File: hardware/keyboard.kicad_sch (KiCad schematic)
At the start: 65 parts, among them SW1 SW_Push, SW10 SW_Push, SW11 SW_Push, SW12 SW_Push, SW13 SW_Push, SW14 SW_Push, SW15 SW_Push, SW16 SW_Push, SW17 SW_Push, SW18 SW_Push, SW19 SW_Push, SW2 SW_Push, SW20 SW_Push, SW21 SW_Push, SW22 SW_Push, SW23 SW_Push, SW24 SW_Push, SW25 SW_Push, SW26 SW_Push, SW27 SW_Push, SW28 SW_Push, SW29 SW_Push, SW3 SW_Push, SW30 SW_Push, SW31 SW_Push, SW32 SW_Push, SW33 SW_Push, SW34 SW_Push, SW35 SW_Push, SW36 SW_Push, SW37 SW_Push, SW38 SW_Push, SW39 SW_Push, SW4 SW_Push, SW40 SW_Push, SW41 SW_Push, SW42 SW_Push, SW43 SW_Push, SW44 SW_Push, SW45 SW_Push, SW46 SW_Push, SW47 SW_Push, SW48 SW_Push, SW49 SW_Push, SW5 SW_Push, SW50 SW_Push, SW51 SW_Push, SW52 SW_Push, SW53 SW_Push, SW54 SW_Push, SW55 SW_Push, SW56 SW_Push, SW6 SW_Push, SW7 SW_Push, SW8 SW_Push, SW9 SW_Push, U2 74HC138

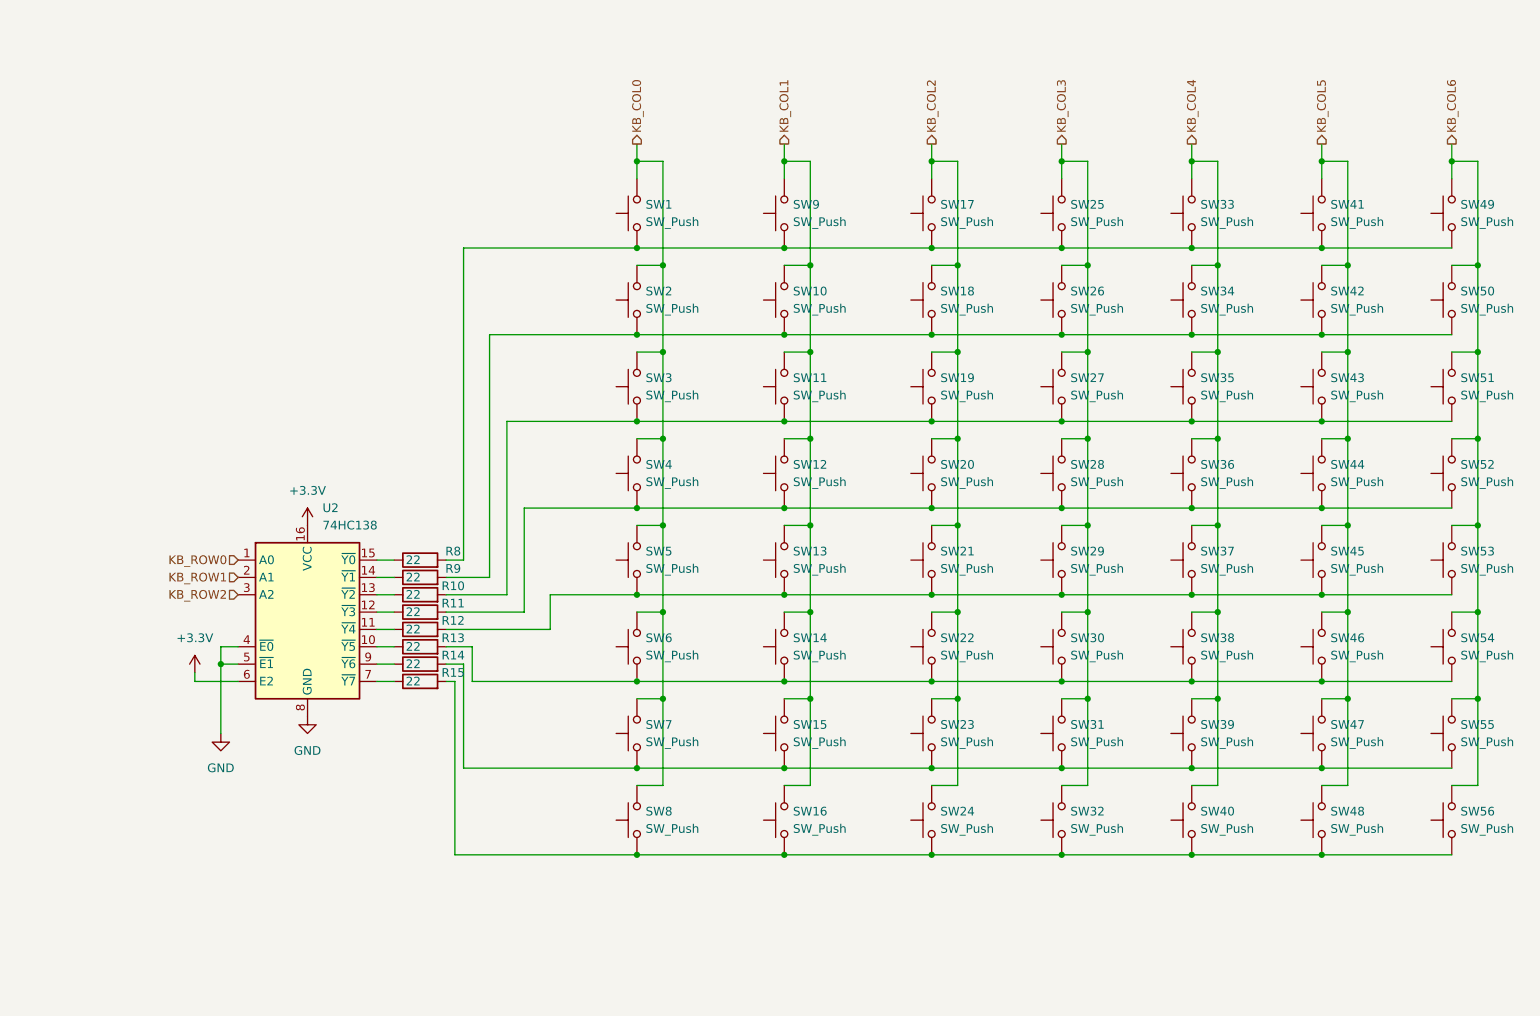
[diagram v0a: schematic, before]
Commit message: joystick collegato, tastiera aggiornata, modulo lora, layout preliminare
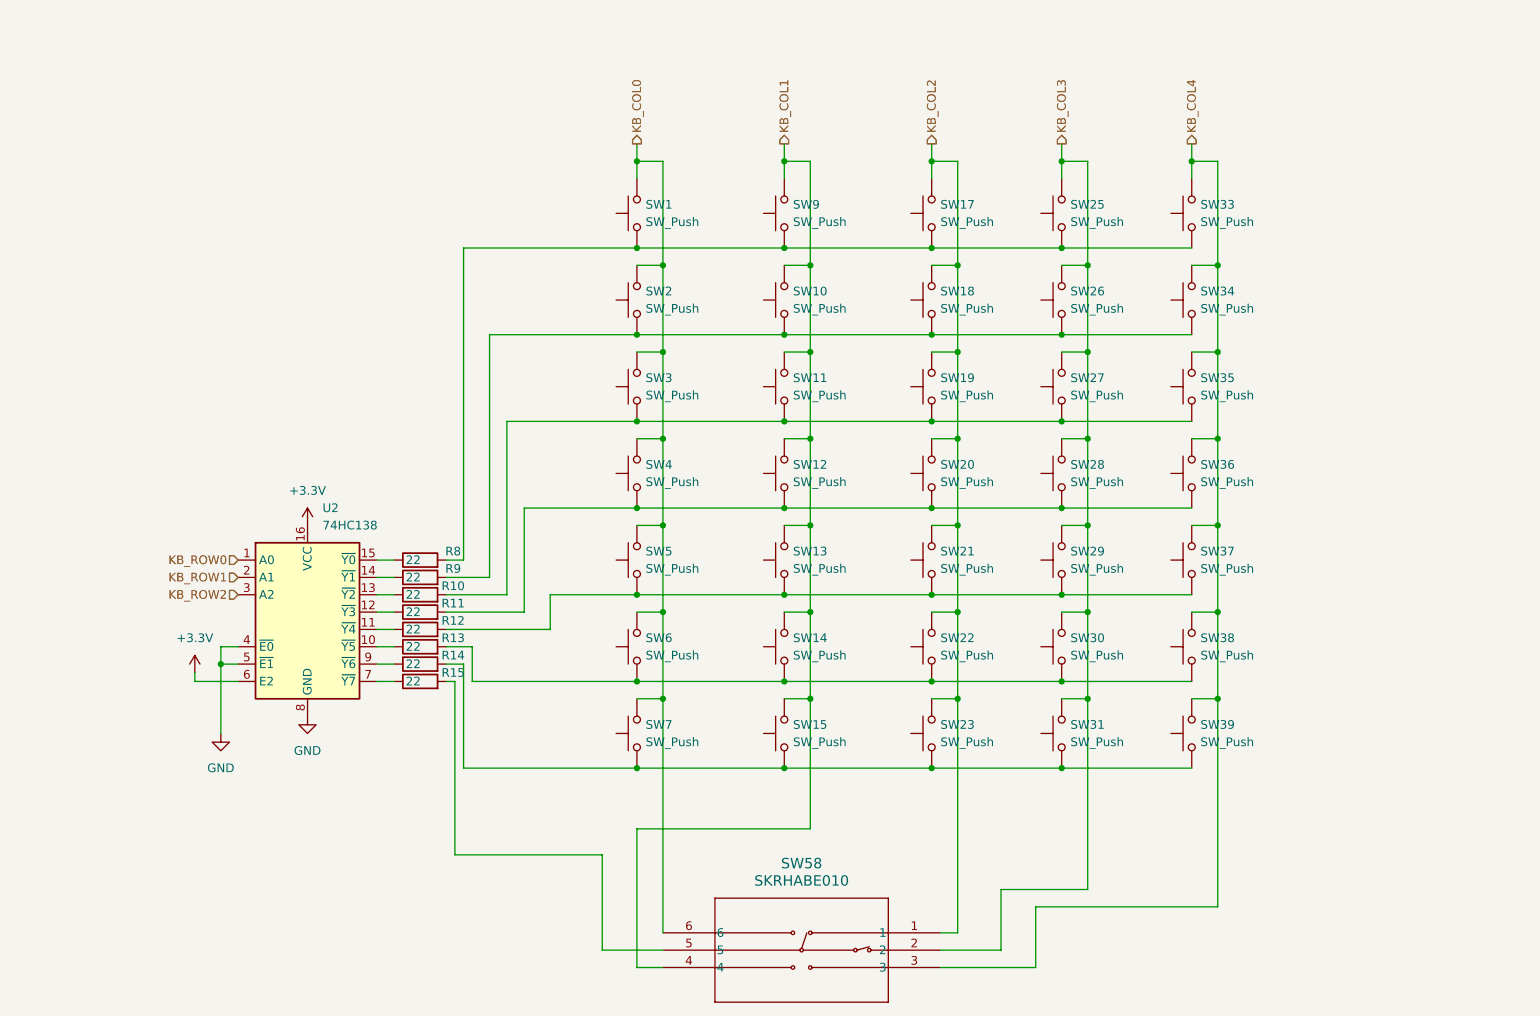
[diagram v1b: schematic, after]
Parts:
- removed SW16, SW24, SW32, SW40, SW41, SW42, SW43, SW44, SW45, SW46, SW47, SW48, SW49, SW50, SW51, SW52, SW53, SW54, SW55, SW56, SW8: SW_Push, lib:bottonepiccolo_C2888430, symbol Switch:SW_Push
- added SW58: SKRHABE010, SKRHABE010_ALPS, symbol 2024-05-18_00-01-46:SKRHABE010
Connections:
- net KB_COL0: now also SW58.6
- net KB_COL1: now also SW58.4
- net KB_COL2: now also SW58.1
- net KB_COL3: now also SW58.2
- net KB_COL4: now also SW58.3
- net at R15.2: now also SW58.5

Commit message: use AO3400A in place of the npn
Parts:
- SW58: footprint SKRHABE010_ALPS -> lib:SKRHABE010_ALPS
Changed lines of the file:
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@@
 			)
 		)
-		(property "Footprint" "SKRHABE010_ALPS"
+		(property "Footprint" "lib:SKRHABE010_ALPS"
 			(at 160.02 163.83 0)
 			(effects

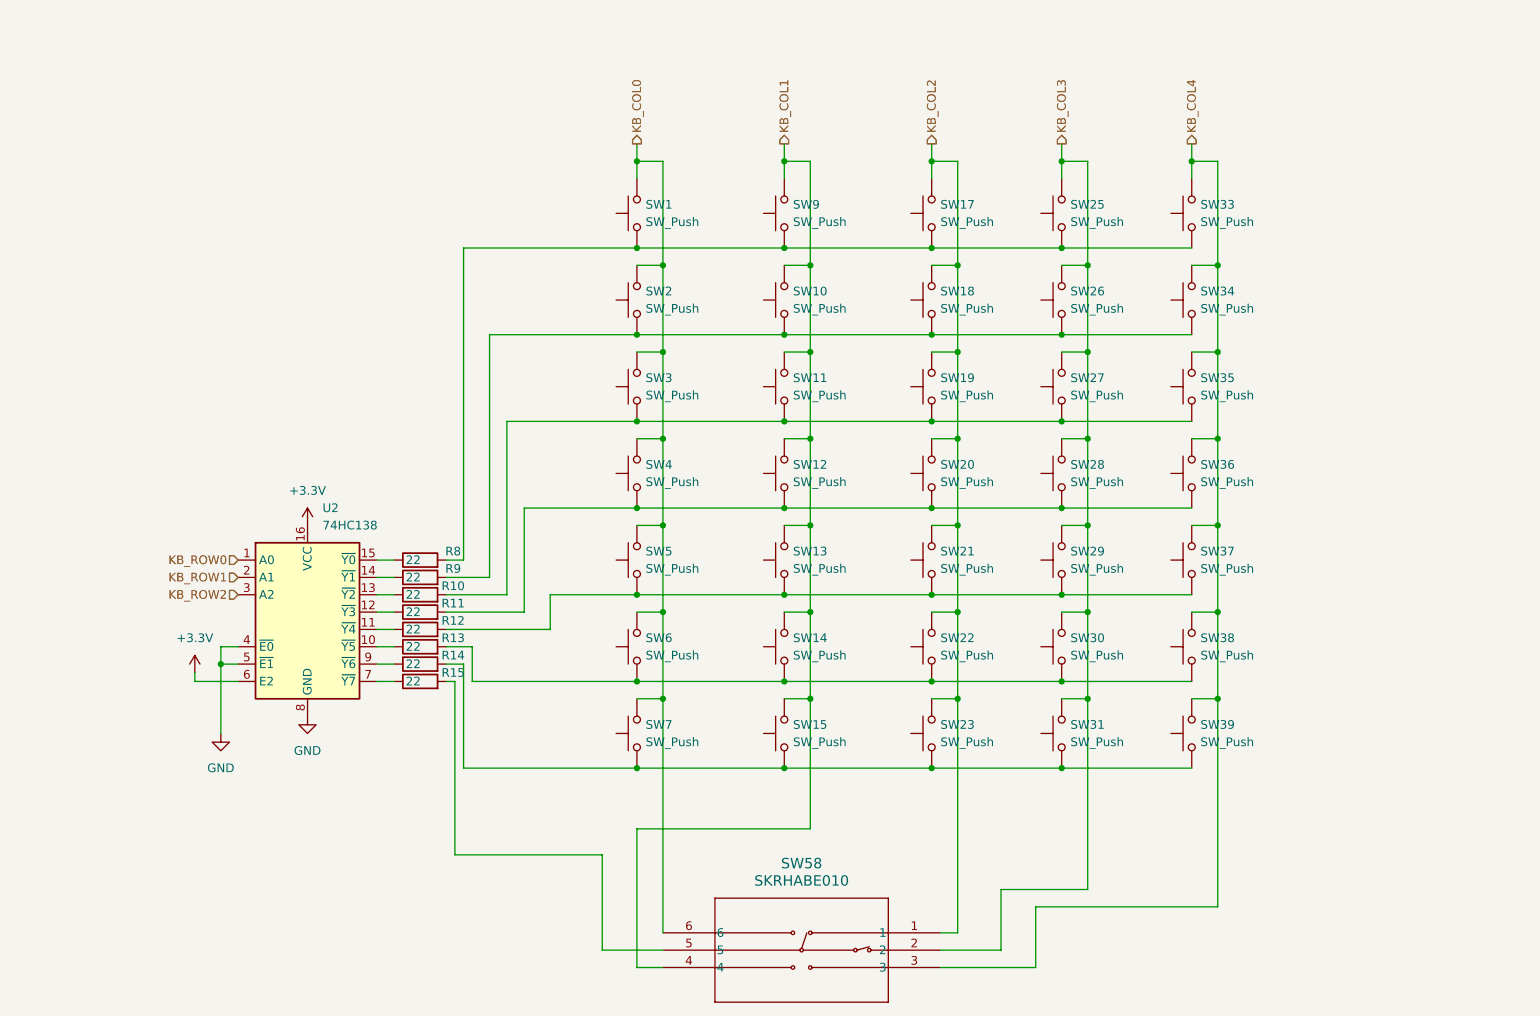
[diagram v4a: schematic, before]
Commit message: remove mux, use i2c expander for keyboard
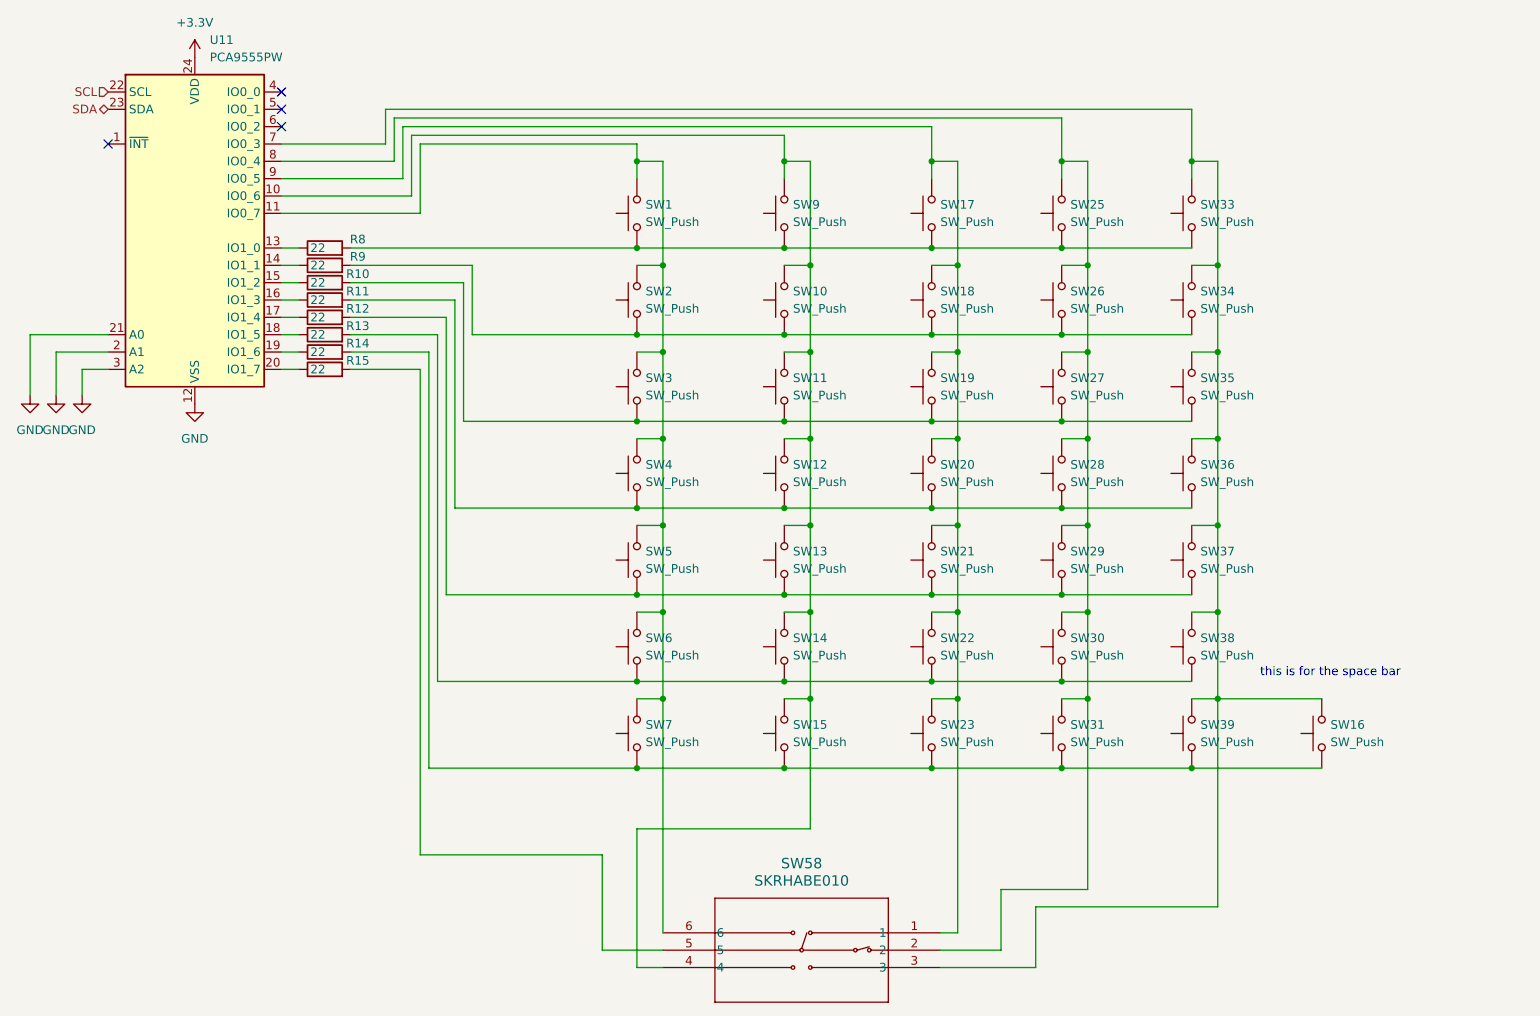
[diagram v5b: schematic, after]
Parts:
- removed U2: 74HC138, Package_SO:SOIC-16_3.9x9.9mm_P1.27mm, symbol 74xx:74HC138
- added SW16: SW_Push, lib:bottonepiccolo_C2888430, symbol Switch:SW_Push
- added U11: PCA9555PW, Package_SO:TSSOP-24_4.4x7.8mm_P0.65mm, symbol Interface_Expansion:PCA9555PW
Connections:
- net +3.3V: now also U11.24 (VDD)
- net GND: now also U11.12 (VSS), U11.2 (A1), U11.21 (A0), U11.3 (A2)
- net at R14.1: now also U11.19 (IO1_6)
- net at R14.2, SW15.1, SW23.1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: now also SW16.1
- net at R9.1: now also U11.14 (IO1_1)
- net at R13.1: now also U11.18 (IO1_5)
- net at R11.1: now also U11.16 (IO1_3)
- net at R8.1: now also U11.13 (IO1_0)
- net at R12.1: now also U11.17 (IO1_4)
- net at R10.1: now also U11.15 (IO1_2)
- net at R15.1: now also U11.20 (IO1_7)
- net KB_COL0: no longer names the net of SW1.2, SW2.2, SW3.2, SW4.2, SW5.2, SW58.6, SW6.2, SW7.2
- net KB_COL0: now also U11.11 (IO0_7)
- net KB_COL1: no longer names the net of SW10.2, SW11.2, SW12.2, SW13.2, SW14.2, SW15.2, SW58.4, SW9.2
- net KB_COL1: now also U11.10 (IO0_6)
- net KB_COL2: no longer names the net of SW17.2, SW18.2, SW19.2, SW20.2, SW21.2, SW22.2, SW23.2, SW58.1
- net KB_COL2: now also U11.9 (IO0_5)
- net KB_COL3: no longer names the net of SW25.2, SW26.2, SW27.2, SW28.2, SW29.2, SW30.2, SW31.2, SW58.2
- net KB_COL3: now also U11.8 (IO0_4)
- net KB_COL4: no longer names the net of SW33.2, SW34.2, SW35.2, SW36.2, SW37.2, SW38.2, SW39.2, SW58.3
- net KB_COL4: now also SW16.2, U11.7 (IO0_3)
- new net SCL: U11.22 (SCL)
- new net SDA: U11.23 (SDA)
- no-connect marks 0 -> 4
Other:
- note added: "this is for the space bar"
- moved on the sheet: R10, R11, R12, R13, R14, R15, R8, R9

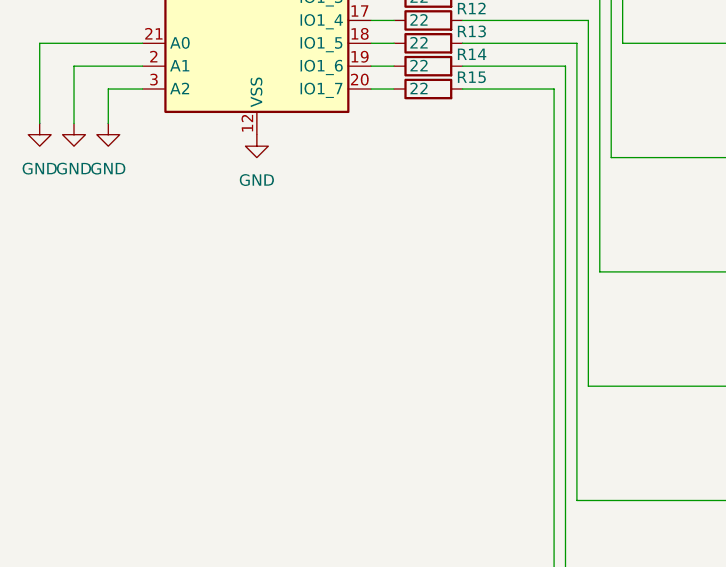
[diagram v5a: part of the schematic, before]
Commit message: Route I2C bus
Add decoupling capacitors to esp32 and io expandes
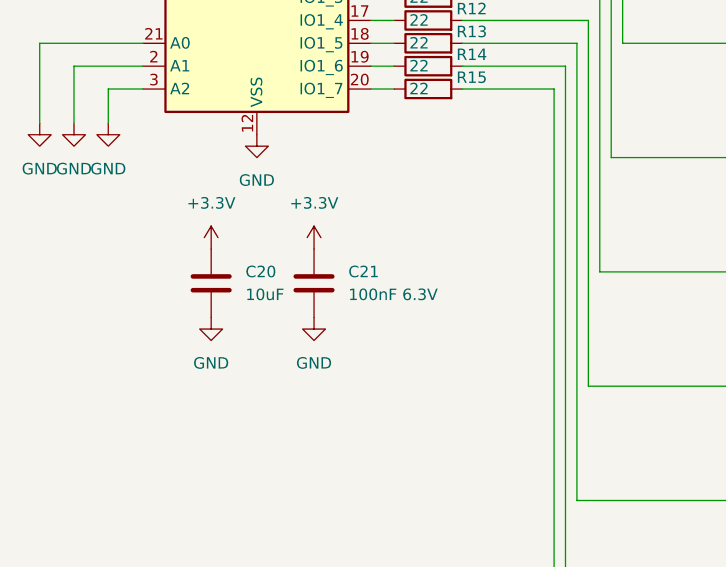
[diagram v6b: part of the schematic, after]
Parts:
- added C20: 10uF, Capacitor_SMD:C_0603_1608Metric, symbol Device:C
- added C21: 100nF 6.3V, Capacitor_SMD:C_0402_1005Metric, symbol Device:C
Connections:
- net +3.3V: now also C20.1, C21.1
- net GND: now also C20.2, C21.2
